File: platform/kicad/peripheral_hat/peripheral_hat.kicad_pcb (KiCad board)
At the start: 4 copper layers, 30 x 65 mm, 49 parts, among them J1 Pi Header, J2 Pogo Pin, J3 Pogo Pin, J4 CRJ032-1-TH, T1 PT61018PEL, U1 LAN9500A-ABZJ, U2 AP63205WU-7

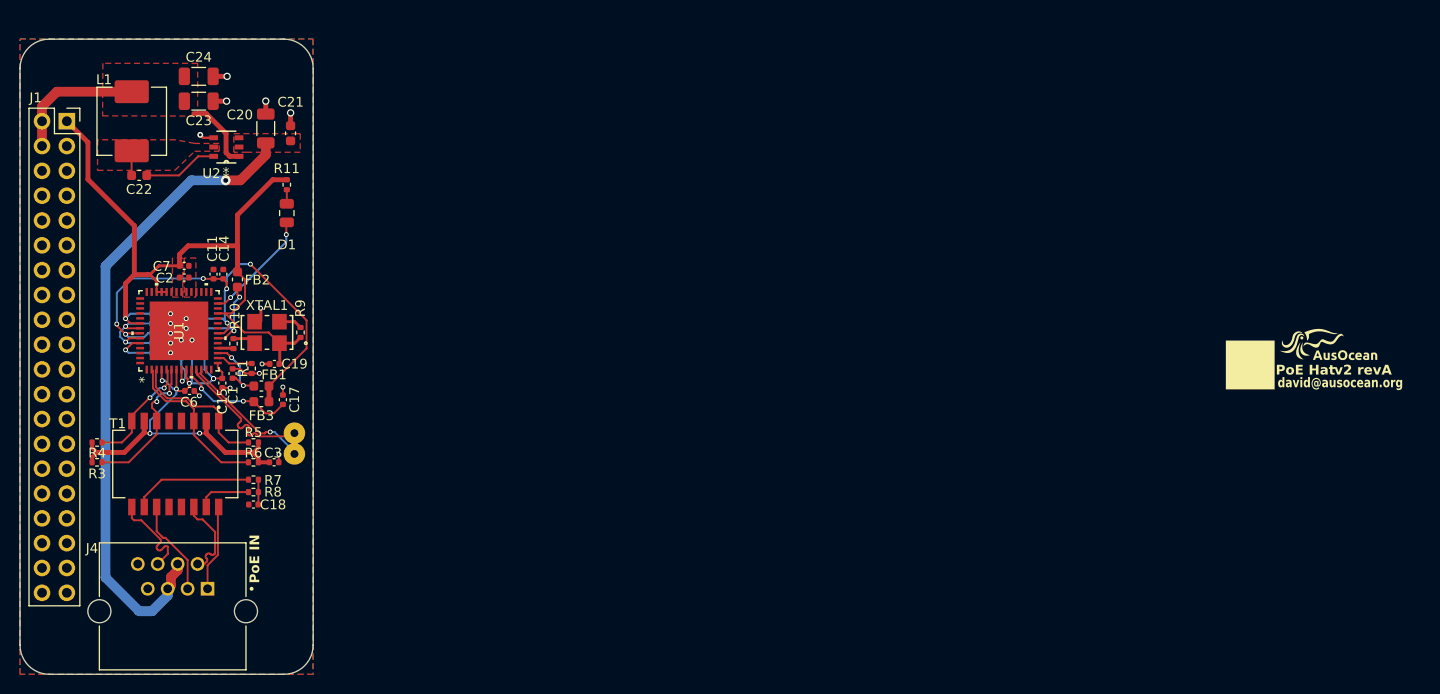
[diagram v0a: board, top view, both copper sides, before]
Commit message: Pi Hat: Make review changes (#23)
This change makes the changes as recommended by the microchip review
service.
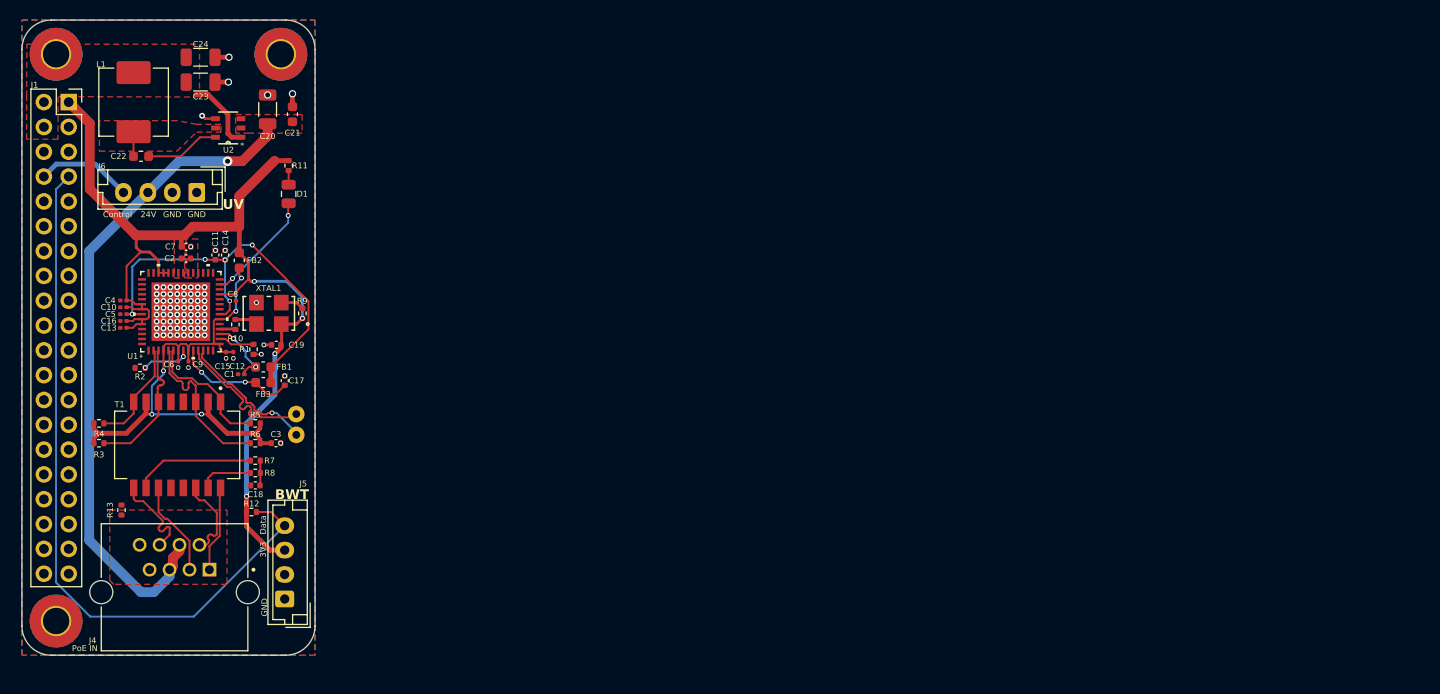
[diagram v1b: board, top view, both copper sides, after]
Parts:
- added H1: MountingHole_Pad, MountingHole:MountingHole_2.7mm_M2.5_Pad_TopBottom, F.Cu at (136.2, 68.5)
- added H2: MountingHole_Pad, MountingHole:MountingHole_2.7mm_M2.5_Pad_TopBottom, F.Cu at (159.2, 68.5)
- added H3: MountingHole_Pad, MountingHole:MountingHole_2.7mm_M2.5_Pad_TopBottom, F.Cu at (136.2, 126.5)
- added J5: JST EH, Connector_JST:JST_EH_B4B-EH-A_1x04_P2.50mm_Vertical, F.Cu at (159.6, 124.3)
- added J6: JST EH, Connector_JST:JST_EH_B4B-EH-A_1x04_P2.50mm_Vertical, F.Cu at (150.6, 82.7)
- added R12: 4k7, Resistor_SMD:R_0402_1005Metric, F.Cu at (156.2, 115.4)
- added R13: 0, Resistor_SMD:R_0402_1005Metric, F.Cu at (142.9, 115.2)
- C1, C15, C6: footprint Capacitor_SMD:C_0402_1005Metric -> Capacitor_SMD:C_0201_0603Metric
- C10, C12, C13, C16, C4, C5, C8, C9: footprint Capacitor_SMD:C_0402_1005Metric -> Capacitor_SMD:C_0201_0603Metric; moved to F.Cu
- G***: moved to B.Cu
- J2, J3: footprint AusOcean:YZ70115093P-02 -> AusOcean:YZP0009-20130-01
- R2: moved to F.Cu
- moved G*** 121.9 mm to (147.6, 71.0), turned to 180 degrees
- moved C16 4.72 mm to (143.1, 95.8), turned to 180 degrees
- moved R2 4.49 mm to (144.8, 100.6), turned to 0 degrees
- moved C12 4.39 mm to (154.3, 99.3), turned to -90 degrees
- moved C5 3.94 mm to (143.1, 95.1), turned to 180 degrees
- moved C8 3.84 mm to (154.3, 93.8), turned to 0 degrees
- moved C10 3.80 mm to (143.1, 94.4), turned to 180 degrees
- moved C13 3.76 mm to (143.1, 96.5), turned to 180 degrees
- moved C4 3.68 mm to (143.1, 93.7), turned to 180 degrees
- moved C6 2.95 mm to (148.7, 100.3), turned to -90 degrees
- moved C15 2.88 mm to (153.6, 99.3)
- moved C11 1.96 mm to (152.5, 89.1)
- moved C14 1.96 mm to (153.5, 89.1)
- moved C21 1.96 mm to (160.4, 74.7)
- moved C3 1.96 mm to (158.7, 108.3)
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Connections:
- J1 pad 7: unconnected-(J1-Pin_7-Pad7) -> ONEWIRE
- J1 pad 8: unconnected-(J1-Pin_8-Pad8) -> UVCONT
- J4 pad 7: GND -> Net-(J4-Pad7)
- J4 pad 8: GND -> Net-(J4-Pad7)
- R3 pad 1: RD+ -> TD+
- R4 pad 1: RD- -> TD-
- R5 pad 1: TD+ -> RD+
- R6 pad 1: TD- -> RD-
- T1 pad 1: TD+ -> RD+
- T1 pad 3: TD- -> RD-
- T1 pad 6: RD+ -> TD+
- T1 pad 8: RD- -> TD-
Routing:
- net ONEWIRE: track 0.00 -> 74.2 mm
- net +3V3: track 91.5 -> 108.2 mm
- net GND: track 23.3 -> 7.21 mm, vias 21 -> 81
- net +5V: track 21.4 -> 7.60 mm
- net UVCONT: track 0.00 -> 9.87 mm
- net +3.3VA: track 63.9 -> 55.8 mm, vias 9 -> 5
- net VDDCORE: track 52.2 -> 44.3 mm, vias 6 -> 5
- net TD-: track 16.4 -> 10.8 mm
- net RD-: track 11.8 -> 16.8 mm, vias 2 -> 0
- net 24V: track 66.3 -> 68.7 mm
- net RD+: track 15.1 -> 13.4 mm, vias 2 -> 0
- net EXRES: track 3.90 -> 5.02 mm, vias 1 -> 2
- net TD+: track 14.9 -> 14.3 mm
- net USBD+: track 13.7 -> 14.4 mm
- added copper zone on F.Cu, net Net-(J4-Pad7)
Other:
- board text added: "24V"
- board text added: "3V3"
- board text added: "BWT"
- board text added: "Control"
- board text added: "Data"
- board text added: "GND"
- board text added: "UV"

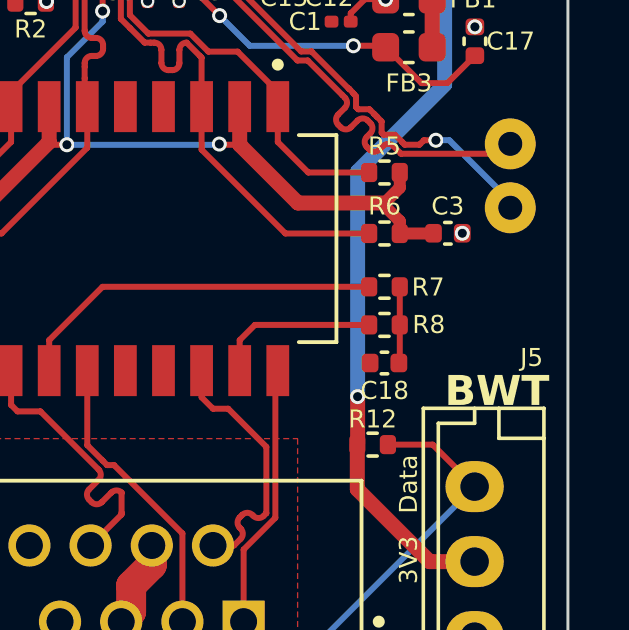
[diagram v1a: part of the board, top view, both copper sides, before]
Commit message: p_HAT: Clean up project files
This change just cleans up which files were being tracked and the
organisation of the files.
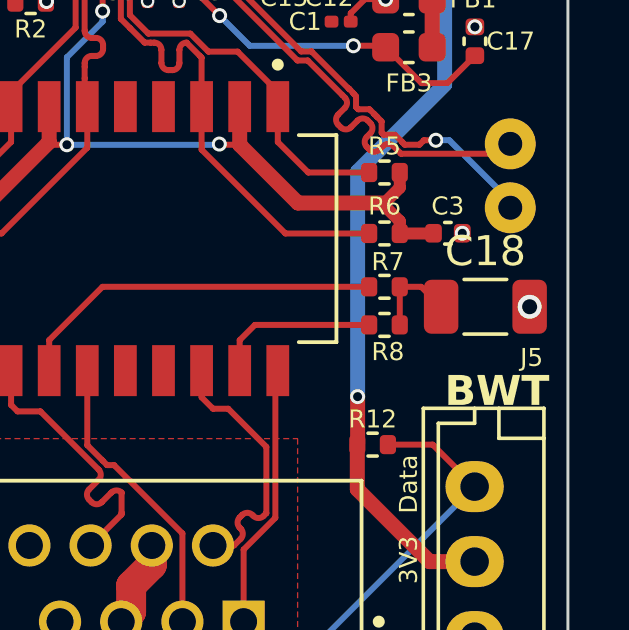
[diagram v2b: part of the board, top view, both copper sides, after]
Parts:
- C18: footprint Capacitor_SMD:C_0402_1005Metric -> Capacitor_SMD:C_1206_3216Metric
- moved C18 3.85 mm to (159.9, 110.8), turned to 0 degrees
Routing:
- net GND: track 7.21 -> 7.42 mm, vias 81 -> 82
